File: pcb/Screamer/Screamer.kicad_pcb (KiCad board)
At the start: 2 copper layers, 52 x 63 mm, 43 parts, among them J1 Conn_01x04, Q1 BC846, U1 RC4558

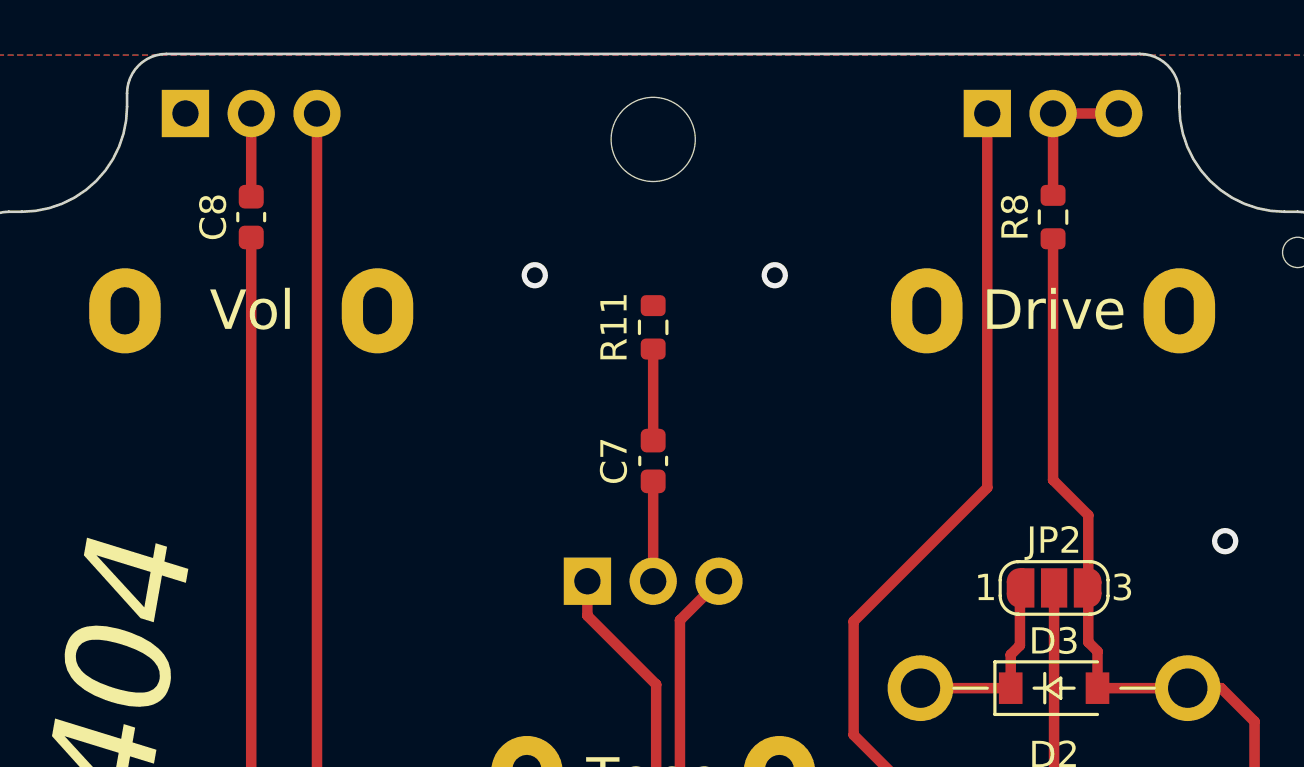
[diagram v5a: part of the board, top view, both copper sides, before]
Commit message: [All] Update all pot footprints and silkscreens
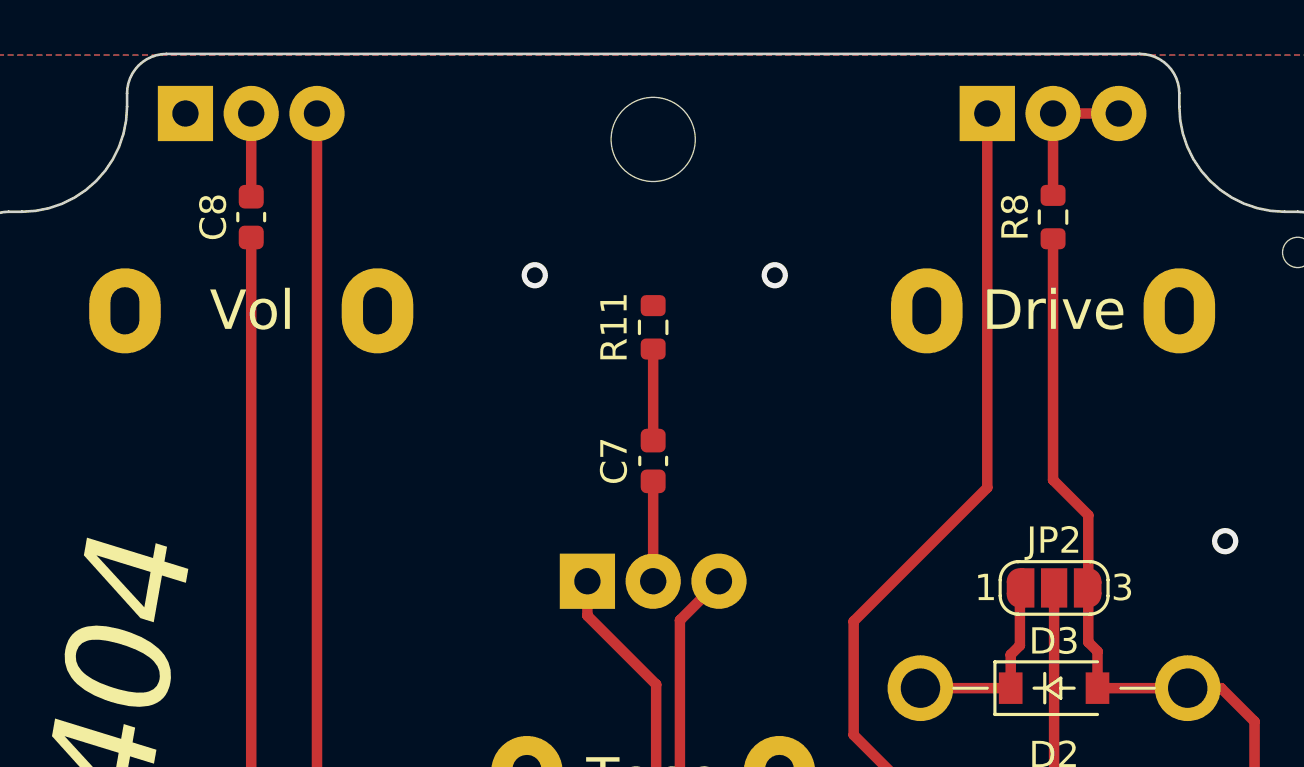
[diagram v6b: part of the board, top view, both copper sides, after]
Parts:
- RV1, RV2, RV3: footprint Potentiometer_THT:Potentiometer_Alpha_RD901F-40-00D_Single_Vertical -> MeineBib:Potentiometer_Alpha_RD901F-40-00D_Single_Vertical
